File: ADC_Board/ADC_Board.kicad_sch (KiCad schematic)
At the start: 25 parts, among them IC1 UCC12040DVE, IC2 ADS131M04QPWRQ1, IC7 ISO7762FDWR, J1 Conn_01x01_Pin, J2 Conn_01x01_Pin, J3 Conn_01x01_Pin, J4 Conn_01x01_Pin, J5 Conn_01x01_Pin, J6 Conn_01x01_Pin, J7 Conn_01x01_Pin, J8 Conn_01x01_Pin, U5 Nucleo_L432KC

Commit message: made changes to layout and schematic
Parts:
- removed C5, C7: 10u, Capacitor_SMD:C_0805_2012Metric, symbol Device:C
- removed C6, C8: 0.1u, Capacitor_SMD:C_0805_2012Metric, symbol Device:C
- removed IC1: UCC12040DVE, UCC12040DVE:SO_0DVER_TEX, symbol UCC12040DVE:UCC12040DVE
- removed J3, J6, J7, J8: Conn_01x01_Pin, UTSVT_Connectors:Banana_Jack_1_Pin_4mm, symbol Connector:Conn_01x01_Pin
- added D5: Power_LED, LED_SMD:LED_0805_2012Metric, symbol Device:LED
- added F1, F2: Fuse, Fuse:Fuseholder_Blade_Mini_Keystone_3568, symbol Device:Fuse
- added R7: 3k, Resistor_SMD:R_1206_3216Metric_Pad1.30x1.75mm_HandSolder, symbol Device:R
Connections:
- net +5V: now also R7.1
- net ARR+: now also F1.1
- net BATTERY+: now also F2.1
- net GND: now also D5.1 (K)
- new net: D5.2 (A), R7.2
- new net ARR+_IN: F1.2
- new net BATT+_IN: F2.2
- no-connect marks 23 -> 22
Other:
- added sheet Power_Isolation (Power_Isolation.kicad_sch)
- sheet Array_Sensors ports: added +ARR_IN, BATT+_IN; removed +ARR, +BATT
- note added: "*Board Notes* Lots of power coming from outside of the board. For the sake of simplicity the devboard won't worry about converting the 12v fusebox to 3.3 and 5v. This will be addressed when all MPPT devboards come together and I can fully design the power architecture."
- note removed: "3V_INPUT"
- note removed: "5V ISOLATOR"
- note removed: "5V_INPUT"

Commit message: Addressed Ravi's Review
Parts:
- added D6: 3.3v_LED, LED_SMD:LED_0805_2012Metric, symbol Device:LED
- added J3, J6: Conn_01x08_Pin, Connector_PinHeader_2.54mm:PinHeader_1x08_P2.54mm_Vertical, symbol Connector:Conn_01x08_Pin
- added R8: 2k, Resistor_SMD:R_1206_3216Metric_Pad1.30x1.75mm_HandSolder, symbol Device:R
- added TP1, TP2, TP3, TP4, TP7, TP8: TestPoint, UTSVT_Special:TestPoint_HEX_3mmID, symbol Connector:TestPoint
- D5: value Power_LED -> 5v_LED
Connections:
- net +3.3V: now also R8.1, TP1.1
- net +5V: now also J6.1 (Pin_1), TP3.1
- net +5V_I: now also J3.1 (Pin_1), TP7.1
- net ADC_DRIVER_CLK: now also J6.2 (Pin_2)
- net ADC_DRIVER_CLK_I: now also J3.2 (Pin_2)
- net DRDY: now also J6.7 (Pin_7)
- net DRDY_I: now also J3.7 (Pin_7)
- net GND: now also D6.1 (K), J6.8 (Pin_8), TP2.1, TP4.1
- net GND_I: now also J3.8 (Pin_8), TP8.1
- net MISO: now also J6.6 (Pin_6)
- net MISO_I: now also J3.6 (Pin_6)
- net MOSI: now also J6.3 (Pin_3)
- net MOSI_I: now also J3.3 (Pin_3)
- net SPI_CLOCK: now also J6.4 (Pin_4)
- net SPI_CLOCK_I: now also J3.4 (Pin_4)
- net SYNC/RESET: now also J6.5 (Pin_5)
- net SYNC/RESET_I: now also J3.5 (Pin_5)
- new net: D6.2 (A), R8.2
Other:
- note added: "Pin Headers for SPI Debug"
- note removed: "*Board Notes* Lots of power coming from outside of the board. For the sake of simplicity the devboard won't worry about converting the 12v fusebox to 3.3 and 5v. This will be addressed when all MPPT devboards come together and I can fully design the power architecture."
- moved on the sheet: F1, F2

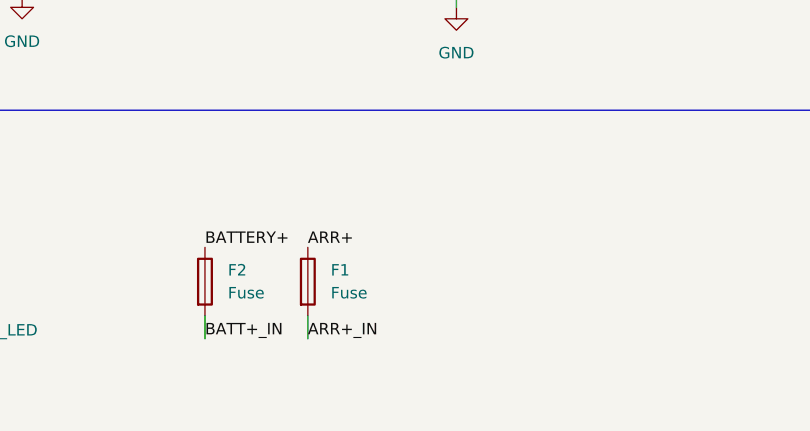
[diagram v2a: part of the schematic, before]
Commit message: Fixed LDO pad, moved bypass caps, added more stitching vias, and cleaned up some silkscreen stuff
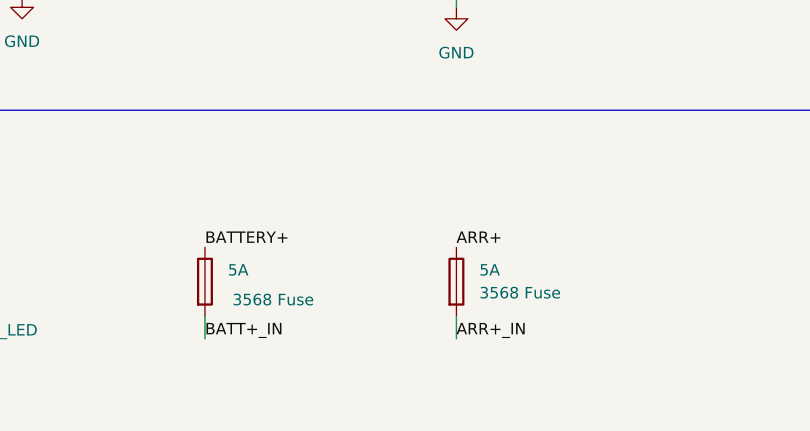
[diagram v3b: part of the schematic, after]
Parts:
- 5A: renamed from F1; value Fuse -> 3568 Fuse
- 5A: renamed from F2; value Fuse -> 3568 Fuse
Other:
- moved on the sheet: 5A
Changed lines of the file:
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@@
 	(wire
 		(pts
-			(xy 80.01 186.69) (xy 80.01 184.15)
+			(xy 96.52 186.69) (xy 96.52 184.15)
 		)
 		(stroke
@@
 	)
 	(label "ARR+_IN"
-		(at 80.01 186.69 0)
+		(at 96.52 186.69 0)
 		(fields_autoplaced yes)
 		(effects
@@
 	)
 	(label "ARR+"
-		(at 80.01 176.53 0)
+		(at 96.52 176.53 0)
 		(fields_autoplaced yes)
 		(effects
@@
 	(symbol
 		(lib_id "Device:Fuse")
-		(at 80.01 180.34 0)
+		(at 96.52 180.34 0)
 		(unit 1)
 		(exclude_from_sim no)
@@
 		(dnp no)
 		(fields_autoplaced yes)
-		(property "Reference" "F1"
-			(at 82.55 179.0699 0)
-			(effects
-				(font
-					(size 1.27 1.27)
-				)
-				(justify left)
-			)
-		)
-		(property "Value" "Fuse"
-			(at 82.55 181.6099 0)
+		(property "Reference" "5A"
+			(at 99.06 179.0699 0)
+			(effects
+				(font
+					(size 1.27 1.27)
+				)
+				(justify left)
+			)
+		)
+		(property "Value" "3568 Fuse"
+			(at 99.06 181.6099 0)
 			(effects
 				(font
@@
 		)
 		(property "Footprint" "Fuse:Fuseholder_Blade_Mini_Keystone_3568"
-			(at 78.232 180.34 90)
+			(at 94.742 180.34 90)
 			(effects
 				(font
@@
 		)
 		(property "Datasheet" "~"
-			(at 80.01 180.34 0)
+			(at 96.52 180.34 0)
 			(effects
 				(font
@@
 		)
 		(property "Description" "Fuse"
-			(at 80.01 180.34 0)
+			(at 96.52 180.34 0)
 			(effects
 				(font
@@
 			(project ""
 				(path "/c2f67899-b13b-465e-9c4c-85240262cdf4"
-					(reference "F1")
+					(reference "5A")
 					(unit 1)
 				)
@@
 		(on_board yes)
 		(dnp no)
-		(fields_autoplaced yes)
-		(property "Reference" "F2"
+		(property "Reference" "5A"
 			(at 71.12 179.0699 0)
 			(effects
@@
 			)
 		)
-		(property "Value" "Fuse"
-			(at 71.12 181.6099 0)
+		(property "Value" "3568 Fuse"
+			(at 71.628 182.372 0)
 			(effects
 				(font
@@
 			(project "ADC_Board"
 				(path "/c2f67899-b13b-465e-9c4c-85240262cdf4"
-					(reference "F2")
-					(unit 1)
-				)
+					(reference "5A")
+					(unit 1)
+				)
